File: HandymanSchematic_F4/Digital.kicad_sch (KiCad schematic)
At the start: 36 parts, among them J1 SWD Header, J2 Jacks, J5 ScopeGroundLoop, Q2 2N7002, Q3 2N7002, SW1 RST, SW2 BYP, U1 ST7789_240x240, U3 STM32F411RETx, U4 AMS1117, Y1 16MHz

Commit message: banished st7789
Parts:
- removed C20: 10u, Capacitor_SMD:C_0805_2012Metric, symbol Device:C
- removed U1: ST7789_240x240, Display:TFT_ST7789_240x240_Breakout, symbol Display_Graphic:TFT_ST7789_240x240_OffBoard
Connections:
- net DISP_BKL: no longer names the net of U3.3 (PC14)
- net DISP_CLK: no longer names the net of U3.55 (PB3)
- net DISP_CS: no longer names the net of U3.2 (PC13)
- net DISP_DC: no longer names the net of U3.62 (PB9)
- net DISP_MOSI: no longer names the net of U3.57 (PB5)
- net DISP_RST: no longer names the net of U3.58 (PB6)
- no-connect marks 33 -> 39
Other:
- note added: "LEDs and OLED display"
- note removed: "LEDs and TFT display"

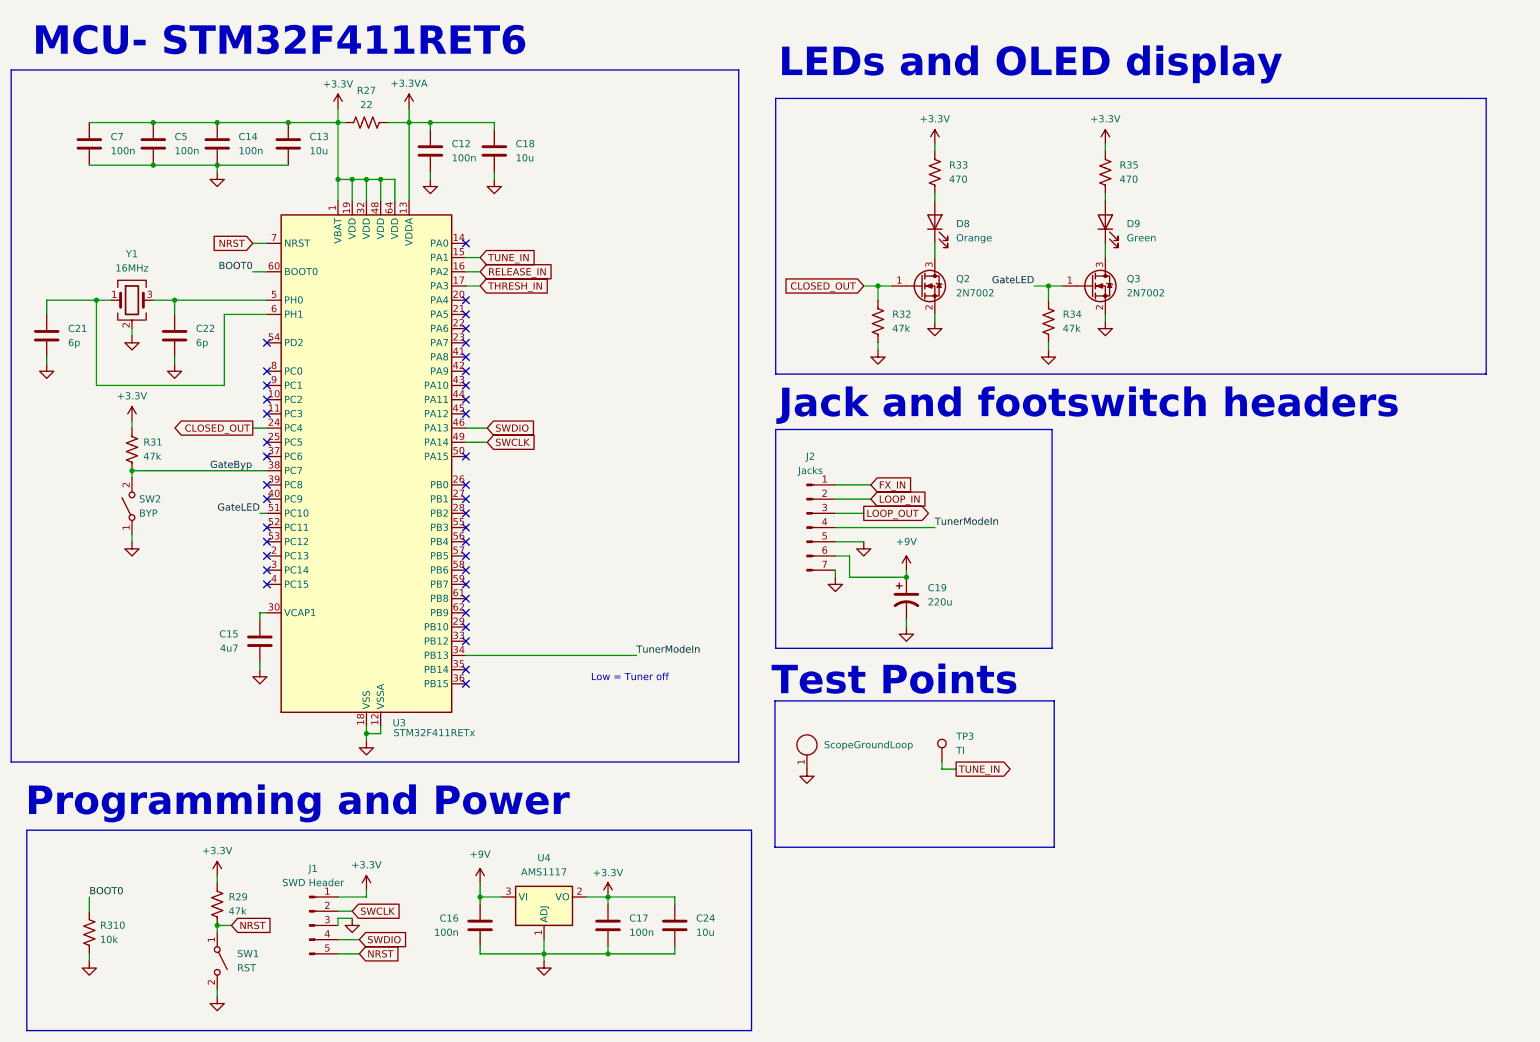
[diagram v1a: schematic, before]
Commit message: switched to 1.3 inch oled
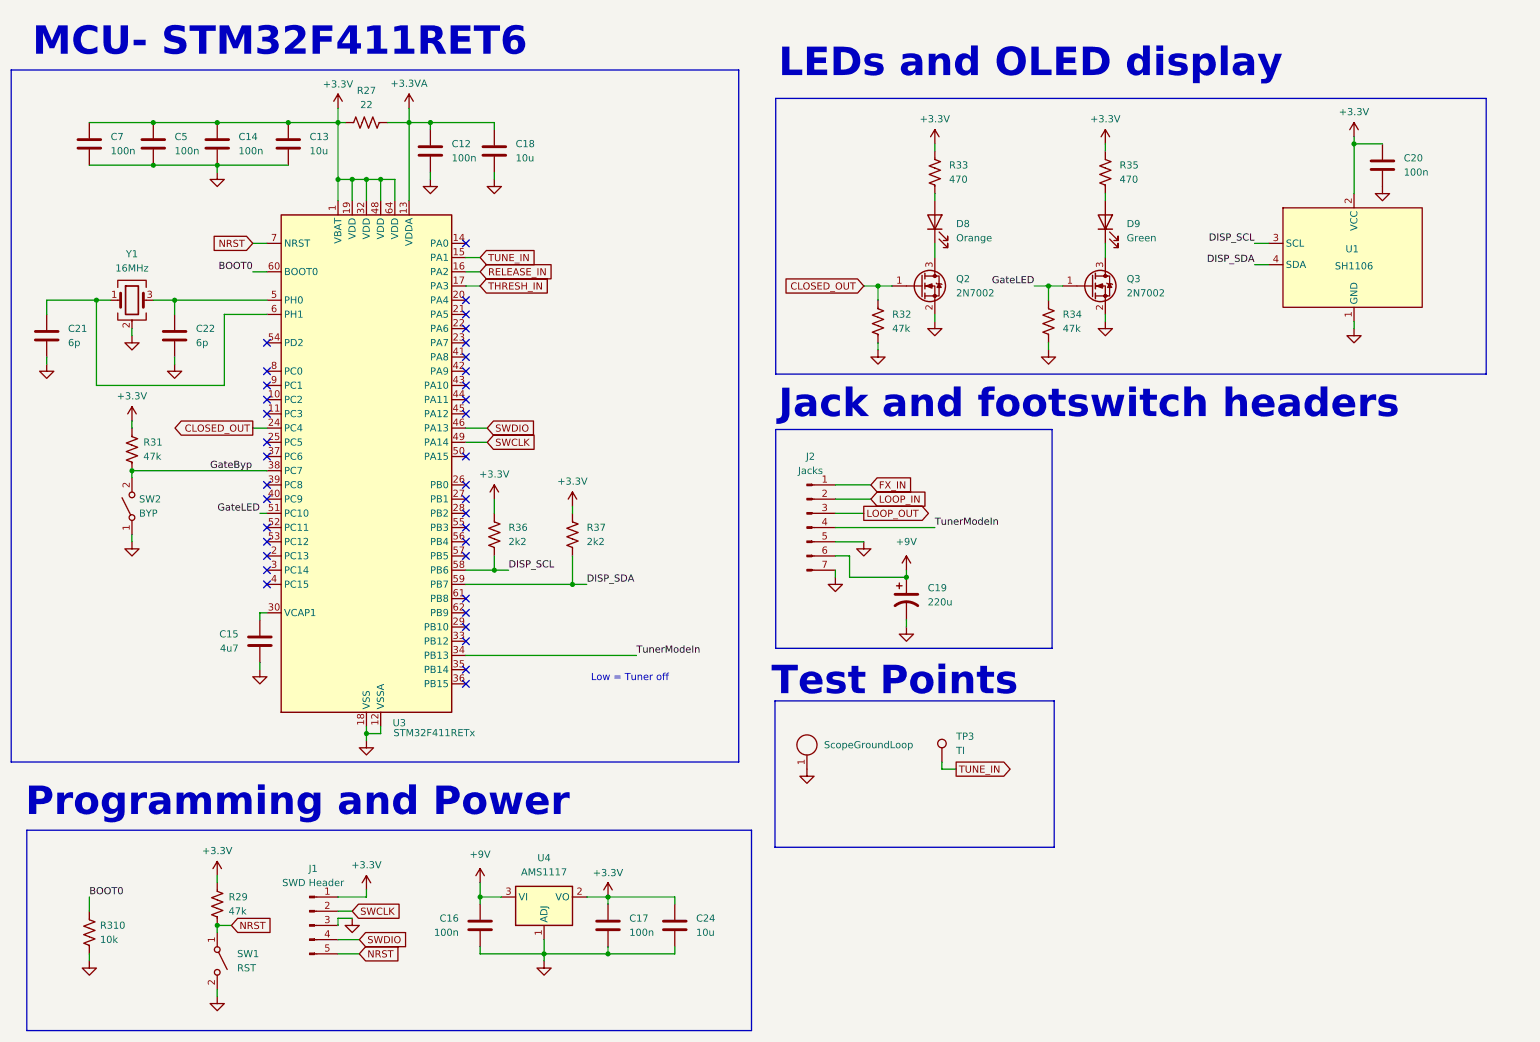
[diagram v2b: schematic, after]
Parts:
- added C20: 100n, Capacitor_SMD:C_0805_2012Metric, symbol Device:C
- added R36, R37: 2k2, Resistor_SMD:R_0805_2012Metric, symbol Device:R_US
- added U1: SH1106, Display:OLED_SH1106_13_OffBoard, symbol Display_Graphic:OLED_SH1106_128x64_OffBoard
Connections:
- net +3.3V: now also C20.2, R36.1, R37.1, U1.2 (VCC)
- net GND: now also C20.1, U1.1 (GND)
- net DISP_SCL: now reaches U3.58 (PB6)
- net DISP_SCL: now also R36.2, U1.3 (SCL)
- net DISP_SDA: now reaches U3.59 (PB7)
- net DISP_SDA: now also R37.2, U1.4 (SDA)
- no-connect marks 39 -> 37

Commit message: routed, DRC passing
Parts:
- removed J5: ScopeGroundLoop, Connector:THT_GND_WIRE, symbol Connector:ScopeGroundLoop
- added C8: 100n, Capacitor_SMD:C_0805_2012Metric, symbol Device:C
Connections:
- net +3.3V: now also C8.2
- net GND: now also C8.1
- net GateByp: now also U3.11 (PC3); no longer U3.38 (PC7)
- net GateLED: now also U3.9 (PC1); no longer U3.51 (PC10)
- net RELEASE_IN: now also U3.27 (PB1); no longer U3.16 (PA2)
- net TUNE_IN: now also U3.22 (PA6); no longer U3.15 (PA1)
- no-connect marks 37 -> 36
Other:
- moved on the sheet: C21, C22, R31, R36, R37, SW2, Y1
